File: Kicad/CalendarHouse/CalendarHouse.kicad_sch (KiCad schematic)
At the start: 26 parts, among them J1 Conn_1x6_LED_MOD, J2 Conn_1x6_SD_CARD, Q1 2N7000, Q2 2N7000, SW1 SW_Push, U1 DEVKIT_V1_ESP32-WROOM-32, U2 AZPAM8403

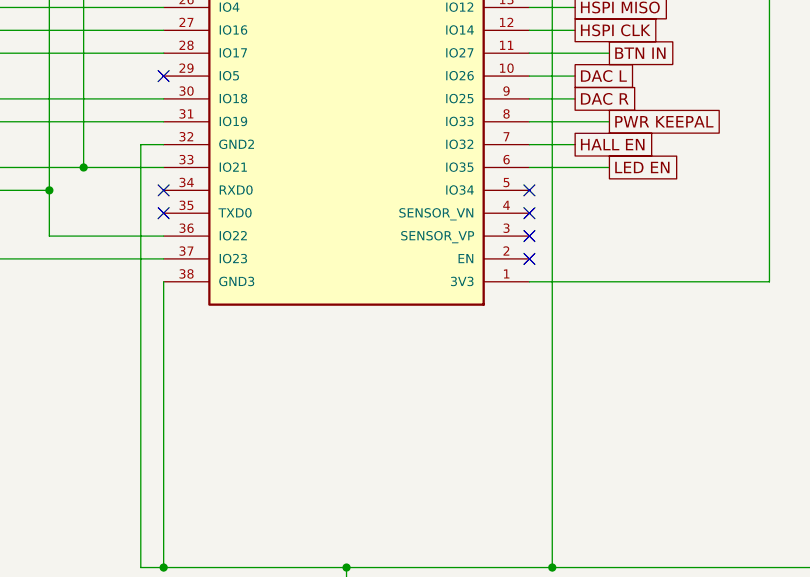
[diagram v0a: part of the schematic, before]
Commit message: PoC LED PWM
- Using Adafruit lib bitbanger
- Cleaned SD Card
- GPIO35 is not suitable for LED_EN
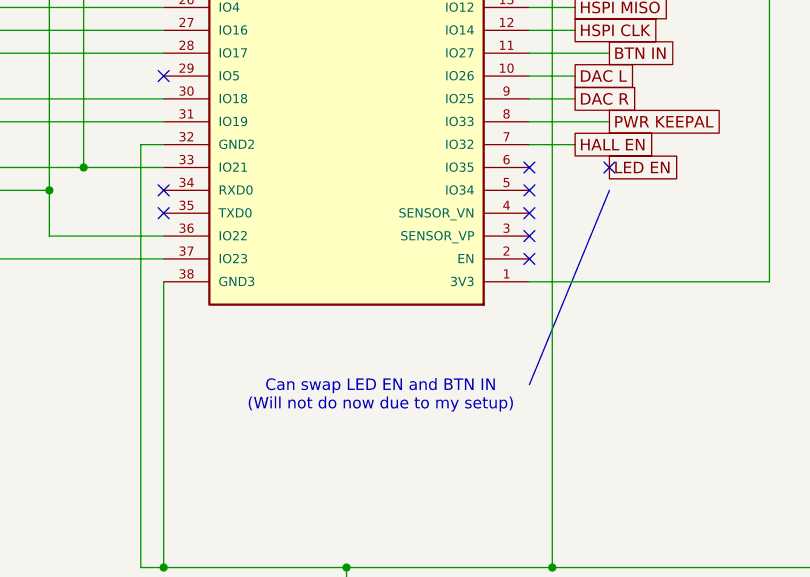
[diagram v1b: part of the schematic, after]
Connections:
- net LED EN: no longer U1.6 (IO35)
- no-connect marks 15 -> 17
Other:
- note added: "Can swap LED EN and BTN IN (Will not do now due to my setup)"
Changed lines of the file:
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@@
+	)
+	(no_connect
+		(at 105.41 78.74)
 	)
 	(no_connect
@@
 	)
 	(no_connect
+		(at 96.52 78.74)
+	)
+	(no_connect
 		(at 55.88 58.42)
 	)
@@
 		)
 	)
+	(polyline
+		(pts
+			(xy 96.52 102.87) (xy 105.41 81.28)
+		)
+		(stroke
+			(width 0)
+			(type default)
+		)
+	)
 	(wire
 		(pts
@@
 		(pts
 			(xy 96.52 58.42) (xy 99.06 58.42)
-		)
-		(stroke
-			(width 0)
-			(type default)
-		)
-	)
-	(wire
-		(pts
-			(xy 96.52 78.74) (xy 105.41 78.74)
 		)
 		(stroke
@@
 		)
 	)
+	(text "Can swap LED EN and BTN IN\n(Will not do now due to my setup)"
+		(exclude_from_sim no)
+		(at 80.01 104.14 0)
+		(effects
+			(font
+				(size 1.27 1.27)
+			)
+		)
+	)

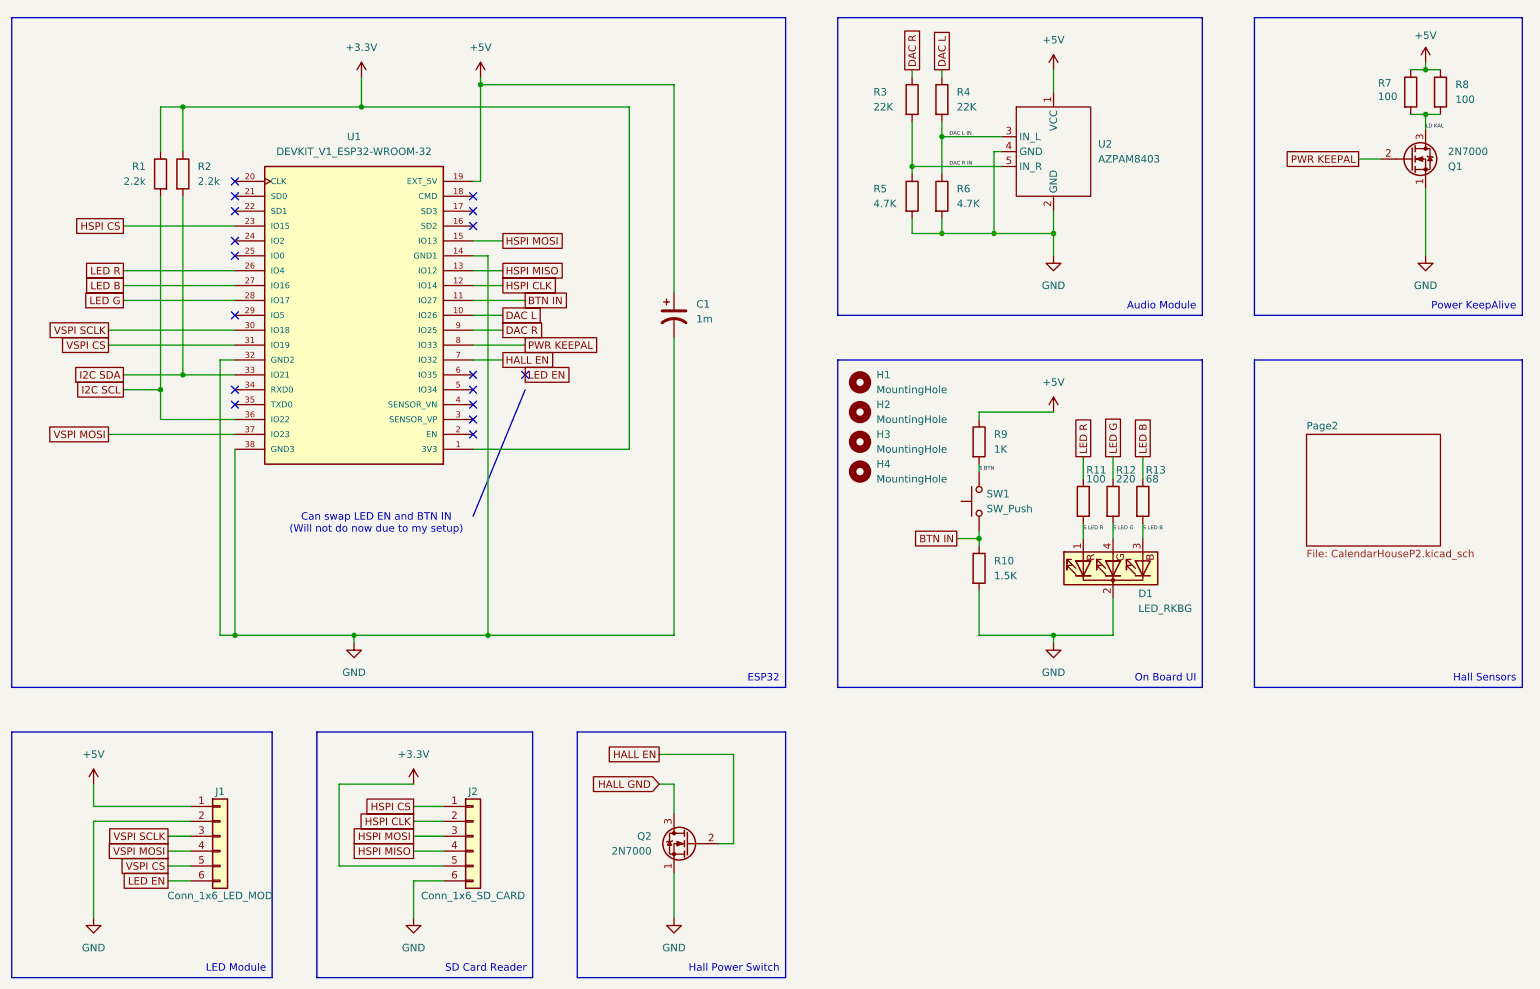
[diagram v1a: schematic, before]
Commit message: Update Schematics due to missing resistor value
- Corrected Design
- New resistors for button due to 1.5k missing in my set
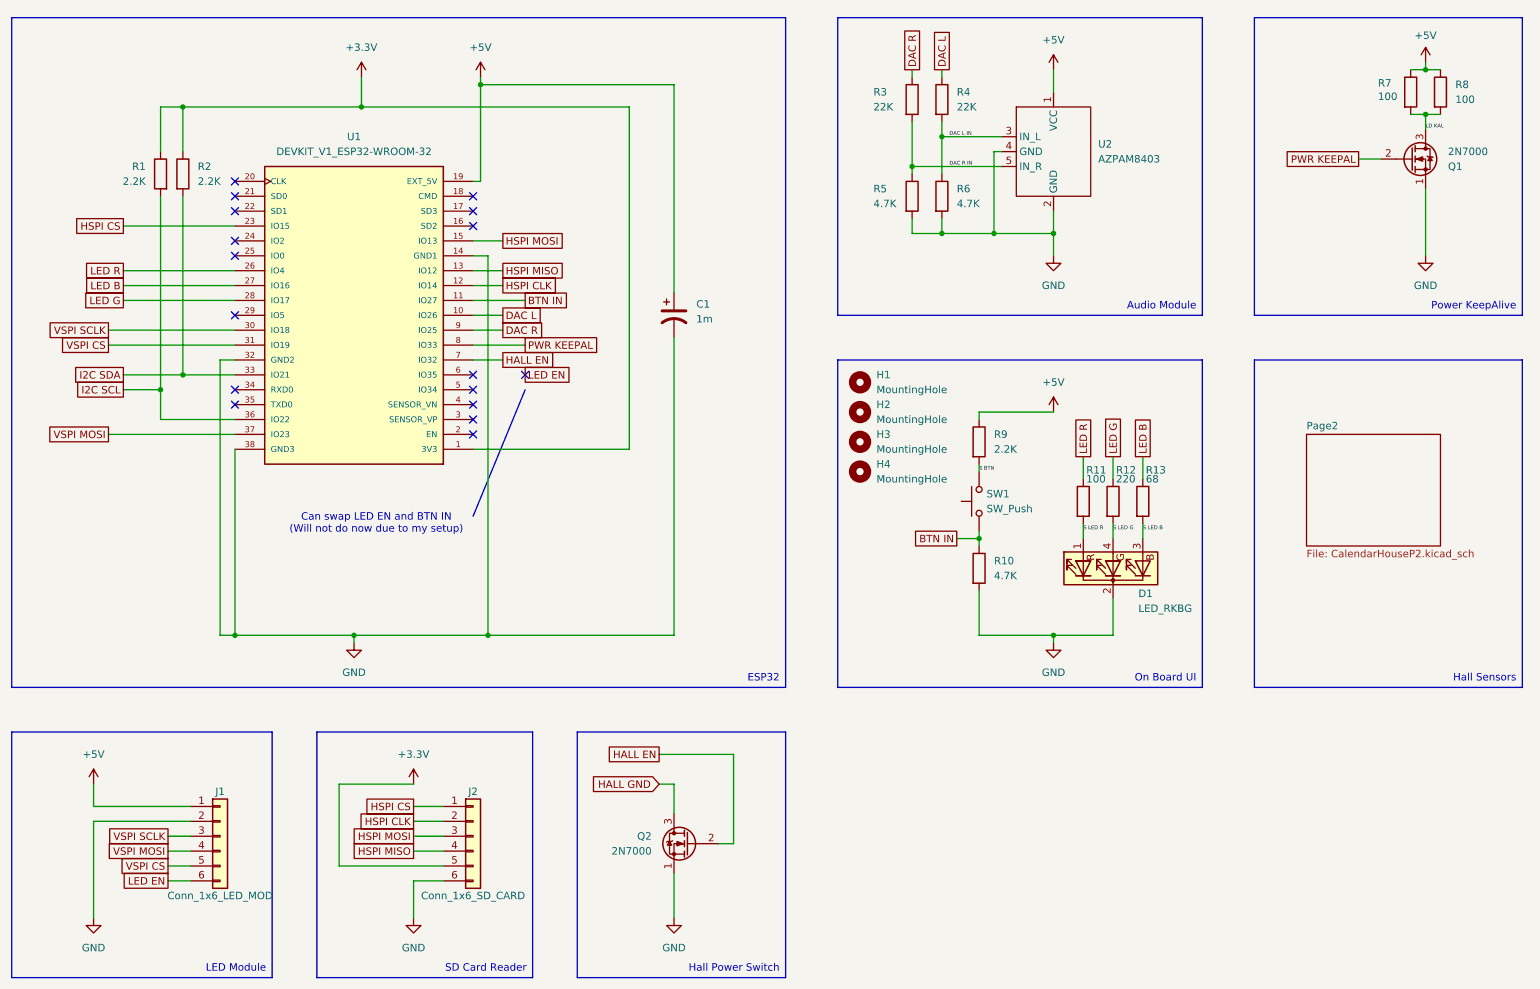
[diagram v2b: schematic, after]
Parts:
- R1, R2: value 2.2k -> 2.2K
- R10: value 1.5K -> 4.7K
- R9: value 1K -> 2.2K
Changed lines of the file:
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@@
 			)
 		)
-		(property "Value" "1.5K"
+		(property "Value" "4.7K"
 			(at 185.42 113.0299 0)
 			(effects
@@
 			)
 		)
-		(property "Value" "2.2k"
+		(property "Value" "2.2K"
 			(at 40.64 45.7199 0)
 			(effects
@@
 			)
 		)
-		(property "Value" "2.2k"
+		(property "Value" "2.2K"
 			(at 49.53 45.7199 0)
 			(effects
@@
 			)
 		)
-		(property "Value" "1K"
+		(property "Value" "2.2K"
 			(at 185.42 91.4399 0)
 			(effects
